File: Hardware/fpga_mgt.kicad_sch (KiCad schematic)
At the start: 0 parts

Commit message: Constraints for BGA layout
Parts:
- added U1: XC7A50T-CPG236, Package_BGA:Xilinx_CPG236, symbol FPGA_Xilinx_Artix7:XC7A50T-CPG236

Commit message: CSG325?
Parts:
- removed U1: XC7A50T-CPG236, Package_BGA:Xilinx_CPG236, symbol FPGA_Xilinx_Artix7:XC7A50T-CPG236
- added R1: 100, Resistor_SMD:R_0402_1005Metric, symbol Device:R
- added U2: XC7A35T-CSG325, Package_BGA:Xilinx_CSG325, symbol FPGA_Xilinx_Artix7:XC7A35T-CSG325

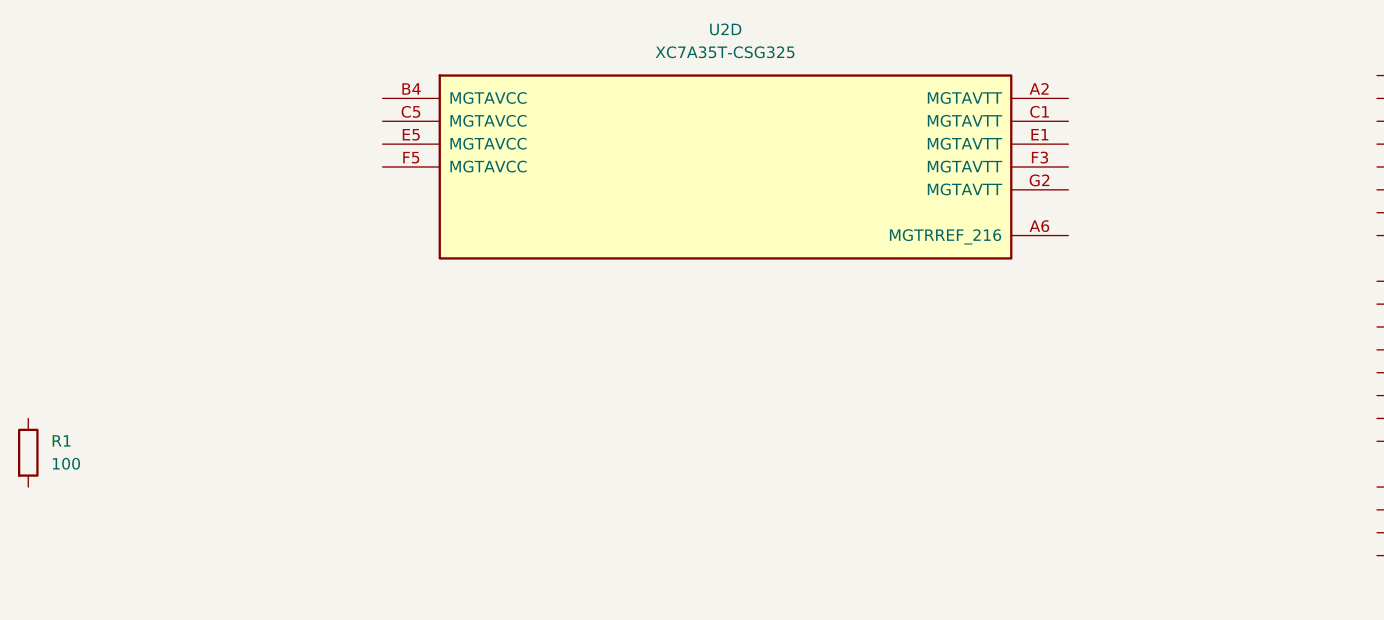
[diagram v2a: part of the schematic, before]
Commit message: Added LGA connector, to be used for configuration interface
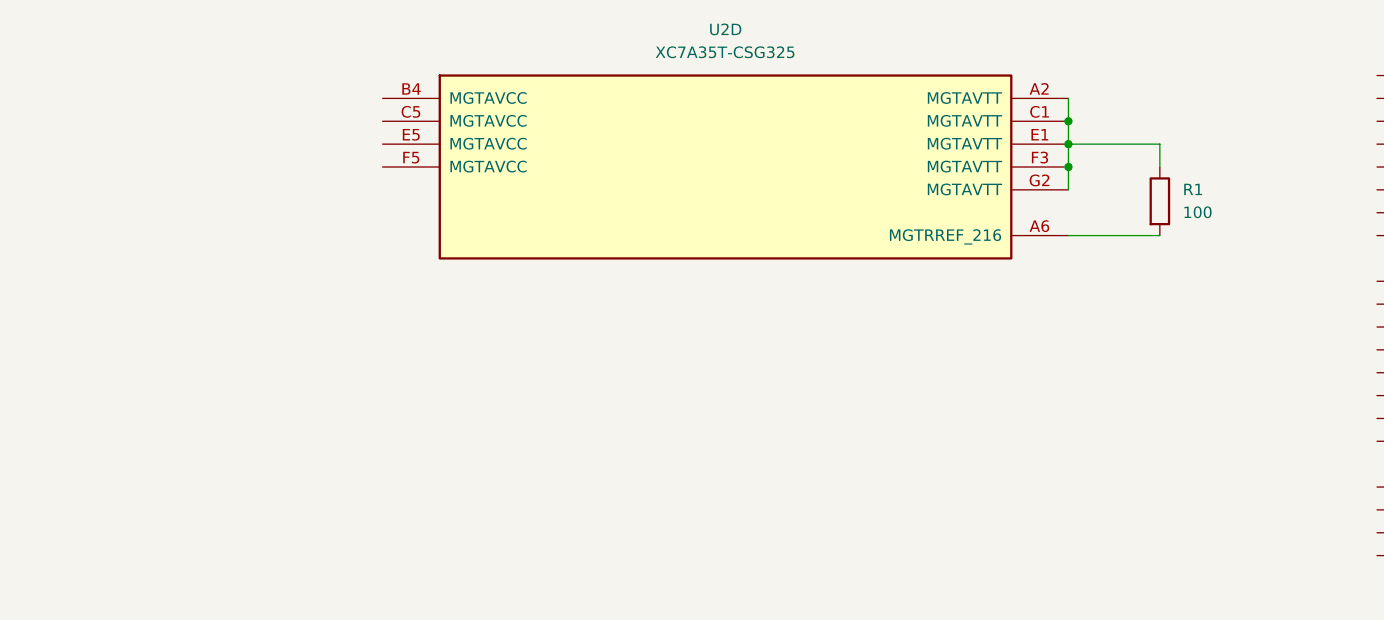
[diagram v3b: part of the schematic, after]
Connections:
- net at U2.A2 (MGTAVTT): now also R1.1, U2.C1 (MGTAVTT), U2.E1 (MGTAVTT), U2.F3 (MGTAVTT), U2.G2 (MGTAVTT)
- net at U2.A6 (MGTRREF_216): now also R1.2
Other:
- moved on the sheet: R1
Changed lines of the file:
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@@
 	(generator_version "10.0")
 	(paper "B")
+	(junction
+		(at 289.56 167.64)
+		(diameter 0)
+		(color 0 0 0 0)
+	)
+	(junction
+		(at 289.56 170.18)
+		(diameter 0)
+		(color 0 0 0 0)
+	)
+	(junction
+		(at 289.56 172.72)
+		(diameter 0)
+		(color 0 0 0 0)
+	)
+	(wire
+		(pts
+			(xy 289.56 172.72) (xy 289.56 175.26)
+		)
+		(stroke
+			(width 0)
+			(type default)
+		)
+	)
+	(wire
+		(pts
+			(xy 289.56 180.34) (xy 299.72 180.34)
+		)
+		(stroke
+			(width 0)
+			(type default)
+		)
+	)
+	(wire
+		(pts
+			(xy 299.72 172.72) (xy 299.72 170.18)
+		)
+		(stroke
+			(width 0)
+			(type default)
+		)
+	)
+	(wire
+		(pts
+			(xy 289.56 167.64) (xy 289.56 170.18)
+		)
+		(stroke
+			(width 0)
+			(type default)
+		)
+	)
+	(wire
+		(pts
+			(xy 299.72 170.18) (xy 289.56 170.18)
+		)
+		(stroke
+			(width 0)
+			(type default)
+		)
+	)
+	(wire
+		(pts
+			(xy 289.56 165.1) (xy 289.56 167.64)
+		)
+		(stroke
+			(width 0)
+			(type default)
+		)
+	)
+	(wire
+		(pts
+			(xy 289.56 170.18) (xy 289.56 172.72)
+		)
+		(stroke
+			(width 0)
+			(type default)
+		)
+	)
 	(symbol
 		(lib_id "FPGA_Xilinx_Artix7:XC7A35T-CSG325")
@@
 	(symbol
 		(lib_id "Device:R")
-		(at 173.99 204.47 0)
+		(at 299.72 176.53 0)
 		(unit 1)
 		(body_style 1)
@@
 		(fields_autoplaced yes)
 		(property "Reference" "R1"
-			(at 176.53 203.1999 0)
+			(at 302.26 175.2599 0)
 			(show_name no)
 			(do_not_autoplace no)
@@
 		)
 		(property "Value" "100"
-			(at 176.53 205.7399 0)
+			(at 302.26 177.7999 0)
 			(show_name no)
 			(do_not_autoplace no)
@@
 		)
 		(property "Footprint" "Resistor_SMD:R_0402_1005Metric"
-			(at 172.212 204.47 90)
+			(at 297.942 176.53 90)
 			(hide yes)
 			(show_name no)
@@
 		)
 		(property "Datasheet" ""
-			(at 173.99 204.47 0)
+			(at 299.72 176.53 0)
 			(hide yes)
 			(show_name no)
@@
 		)
 		(property "Description" "Resistor"
-			(at 173.99 204.47 0)
+			(at 299.72 176.53 0)
 			(hide yes)
 			(show_name no)

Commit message: Trying to assign MGT lanes but I don't know how to do inter sheet connectivity yet
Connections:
- net MGTAVTT: now reaches R1.1, U2.A2 (MGTAVTT), U2.C1 (MGTAVTT), U2.E1 (MGTAVTT), U2.F3 (MGTAVTT), U2.G2 (MGTAVTT)
- net MGTAVCC: now reaches U2.B4 (MGTAVCC)
- net MGTAVCC: now also U2.C5 (MGTAVCC), U2.E5 (MGTAVCC), U2.F5 (MGTAVCC)
- net MGT_SMA_RX_N: now reaches U2.A3 (MGTPRXN1_216)
- net MGT_SMA_RX_P: now reaches U2.A4 (MGTPRXP1_216)
- net PCIE_TX_N: now reaches U2.B1 (MGTPTXN3_216)
- net PCIE_TX_P: now reaches U2.B2 (MGTPTXP3_216)
- net PCIE_CLK_N: now reaches U2.B5 (MGTREFCLK1N_216)
- net PCIE_CLK_P: now reaches U2.B6 (MGTREFCLK1P_216)
- net MGT_LOOPBACK_N: now reaches U2.C3 (MGTPRXN2_216)
- net MGT_LOOPBACK_N: now also U2.D1 (MGTPTXN2_216)
- net MGT_LOOPBACK_P: now reaches U2.C4 (MGTPRXP2_216)
- net MGT_LOOPBACK_P: now also U2.D2 (MGTPTXP2_216)
- net SMA_CLK_N: now reaches U2.D5 (MGTREFCLK0N_216)
- net SMA_CLK_P: now reaches U2.D6 (MGTREFCLK0P_216)
- net MGT_SMA_TX_N: now reaches U2.F1 (MGTPTXN1_216)
- net MGT_SMA_TX_P: now reaches U2.F2 (MGTPTXP1_216)
- net PCIE_RX_N: now reaches U2.G3 (MGTPRXN3_216)
- net PCIE_RX_P: now reaches U2.G4 (MGTPRXP3_216)
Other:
- moved on the sheet: R1, U2D

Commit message: Found the global labels
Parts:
- added J3, J4, J5, J6, J7, J8: Conn_Coaxial, Connector_Coaxial:U.FL_Hirose_U.FL-R-SMT-1_Vertical, symbol Connector:Conn_Coaxial
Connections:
- net PCIE_CLK_N is gone; now on net PCIE_REFCLK_N: U2.B5 (MGTREFCLK1N_216)
- net PCIE_CLK_P is gone; now on net PCIE_REFCLK_P: U2.B6 (MGTREFCLK1P_216)
- net MGT_SMA_RX_N renamed MGT_UFL_RX_N
- net MGT_UFL_RX_N: now also J6.1 (In)
- net MGT_SMA_RX_P renamed MGT_UFL_RX_P
- net MGT_UFL_RX_P: now also J5.1 (In)
- net MGT_SMA_TX_N renamed MGT_UFL_TX_N
- net MGT_UFL_TX_N: now also J4.1 (In)
- net MGT_SMA_TX_P renamed MGT_UFL_TX_P
- net MGT_UFL_TX_P: now also J3.1 (In)
- net SMA_CLK_N renamed UFL_CLK_N
- net UFL_CLK_N: now also J8.1 (In)
- net SMA_CLK_P renamed UFL_CLK_P
- net UFL_CLK_P: now also J7.1 (In)
- new net: J3.2 (Ext), J4.2 (Ext), J5.2 (Ext), J6.2 (Ext), J7.2 (Ext), J8.2 (Ext)

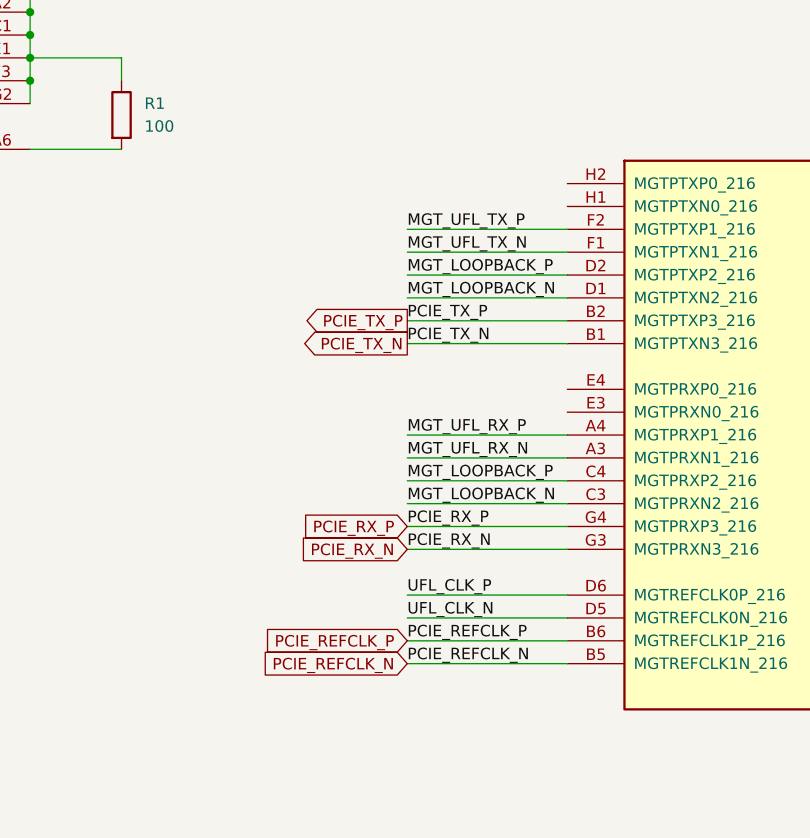
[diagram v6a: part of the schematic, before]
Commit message: This might be better orientation/pin choices
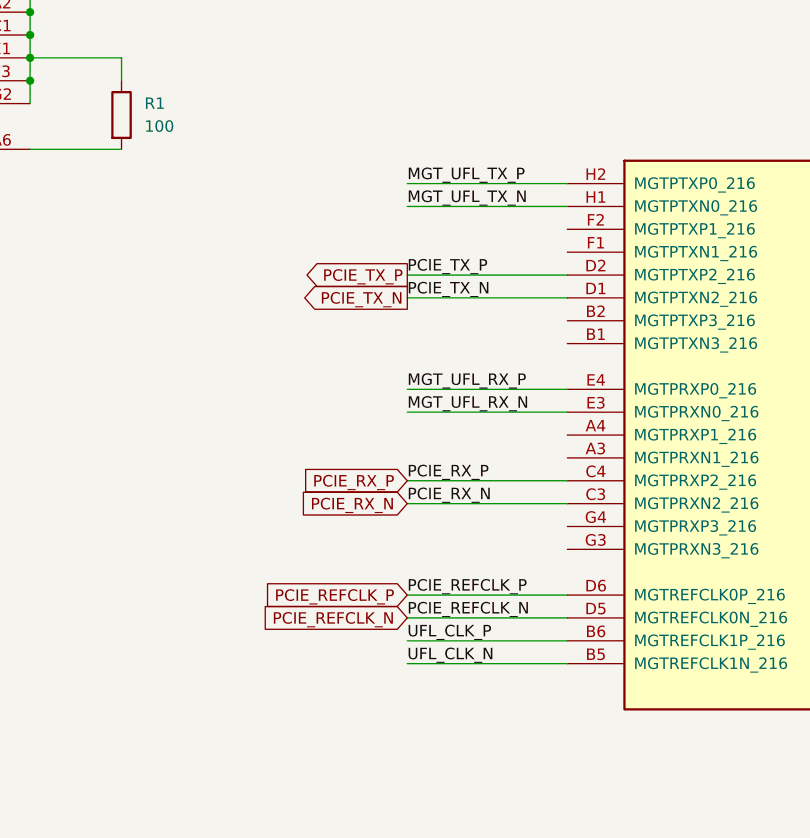
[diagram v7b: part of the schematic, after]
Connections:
- net MGT_UFL_RX_N: now also U2.E3 (MGTPRXN0_216); no longer U2.A3 (MGTPRXN1_216)
- net MGT_UFL_RX_P: now also U2.E4 (MGTPRXP0_216); no longer U2.A4 (MGTPRXP1_216)
- net MGT_UFL_TX_N: now also U2.H1 (MGTPTXN0_216); no longer U2.F1 (MGTPTXN1_216)
- net MGT_UFL_TX_P: now also U2.H2 (MGTPTXP0_216); no longer U2.F2 (MGTPTXP1_216)
- net PCIE_REFCLK_N: now also U2.D5 (MGTREFCLK0N_216); no longer U2.B5 (MGTREFCLK1N_216)
- net PCIE_REFCLK_P: now also U2.D6 (MGTREFCLK0P_216); no longer U2.B6 (MGTREFCLK1P_216)
- net PCIE_RX_N: now also U2.C3 (MGTPRXN2_216); no longer U2.G3 (MGTPRXN3_216)
- net PCIE_RX_P: now also U2.C4 (MGTPRXP2_216); no longer U2.G4 (MGTPRXP3_216)
- net PCIE_TX_N: now also U2.D1 (MGTPTXN2_216); no longer U2.B1 (MGTPTXN3_216)
- net PCIE_TX_P: now also U2.D2 (MGTPTXP2_216); no longer U2.B2 (MGTPTXP3_216)
- net UFL_CLK_N: now also U2.B5 (MGTREFCLK1N_216); no longer U2.D5 (MGTREFCLK0N_216)
- net UFL_CLK_P: now also U2.B6 (MGTREFCLK1P_216); no longer U2.D6 (MGTREFCLK0P_216)
- removed net MGT_LOOPBACK_N: U2.C3 (MGTPRXN2_216), U2.D1 (MGTPTXN2_216)
- removed net MGT_LOOPBACK_P: U2.C4 (MGTPRXP2_216), U2.D2 (MGTPTXP2_216)

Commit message: I gotta find the right regulators
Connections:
- net GND: now reaches J3.2 (Ext), J4.2 (Ext), J5.2 (Ext), J6.2 (Ext), J7.2 (Ext), J8.2 (Ext)
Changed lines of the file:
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@@
+	)
+	(junction
+		(at 201.93 261.62)
+		(diameter 0)
+		(color 0 0 0 0)
 	)
 	(junction
@@
 					(unit 1)
 				)
+			)
+		)
+	)
+	(symbol
+		(lib_id "power:GND")
+		(at 201.93 261.62 0)
+		(unit 1)
+		(body_style 1)
+		(exclude_from_sim no)
+		(in_bom yes)
+		(on_board yes)
+		(in_pos_files yes)
+		(dnp no)
+		(fields_autoplaced yes)
+		(property "Reference" "#PWR040"
+			(at 201.93 267.97 0)
+			(hide yes)
+			(show_name no)
+			(do_not_autoplace no)
+			(effects
+				(font
+					(size 1.27 1.27)
+				)
+			)
+		)
+		(property "Value" "GND"
+			(at 201.93 266.7 0)
+			(show_name no)
+			(do_not_autoplace no)
+			(effects
+				(font
+					(size 1.27 1.27)
+				)
+			)
+		)
+		(property "Footprint" ""
+			(at 201.93 261.62 0)
+			(hide yes)
+			(show_name no)
+			(do_not_autoplace no)
+			(effects
+				(font
+					(size 1.27 1.27)
+				)
+			)
+		)
+		(property "Datasheet" ""
+			(at 201.93 261.62 0)
+			(hide yes)
+			(show_name no)
+			(do_not_autoplace no)
+			(effects
+				(font
+					(size 1.27 1.27)
+				)
+			)
+		)
+		(property "Description" "Power symbol creates a global label with name \"GND\" , ground"
+			(at 201.93 261.62 0)
+			(hide yes)
+			(show_name no)
+			(do_not_autoplace no)
+			(effects
+				(font
+					(size 1.27 1.27)
+				)
+			)
+		)
+		(pin "1"
+		)
+		(instances
+			(project "NotteXCVR"
+				(path "/66cb547b-932d-4f9e-941e-9414e44abcf1/44763f25-dc1a-4528-897f-5ae44a6a44e7"
+					(reference "#PWR040")
+					(unit 1)
+				)
